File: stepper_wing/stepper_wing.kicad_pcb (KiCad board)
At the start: 2 copper layers, 47 x 49.5 mm, 40 parts, among them U1 MCP44X1, U2 MCP23017, U3 DRV8825, U4 DRV8825, U5 DRV8825, U6 DRV8825

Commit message: try alt layout
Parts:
- removed the Nylon Only at (106.4, 80.5)
- removed the Nylon Only at (106.4, 122.4)
- removed WINGPWR1: WINGPWR, Connect:bornier2
- added P1: CONN_1, Local:TabRA, F.Cu at (145.8, 97.0)
- added P2: CONN_1, Local:TabRA, F.Cu at (145.8, 105.9)
- C1, C10, C12, C13, C2, C3, C4, C6, C7, C9: footprint SMD_Packages:SMD-0603_c -> Local:0805C
- C11, C14, C5, C8: footprint SMD_Packages:SMD-0603_c -> Local:0805C; moved to B.Cu
- R1, R2: footprint SMD_Packages:SMD-0603_r -> Local:0805R
- R10, R3, R4, R5, R6, R7, R8, R9: footprint Resistors_SMD:Resistor_SMD2512_HandSoldering -> Resistors_SMD:R_2512
- STEP1, STEP2, STEP3, STEP4: footprint Pin_Headers:Pin_Header_Angled_1x04 -> Pin_Headers:Pin_Header_Straight_1x04
- moved C2 29.8 mm to (110.9, 127.4), turned to 0 degrees
- moved U2 15.9 mm to (109.0, 117.3), turned to 90 degrees
- moved C5 6.91 mm to (121.4, 117.0), turned to 270 degrees
- moved R1 6.59 mm to (114.0, 85.6), turned to 90 degrees
- moved C8 6.56 mm to (121.4, 104.9), turned to 270 degrees
- moved C13 6.35 mm to (126.4, 88.8)
- moved C10 6.26 mm to (126.4, 100.8)
- moved C11 6.25 mm to (121.4, 92.8), turned to 270 degrees
- moved C4 6.23 mm to (126.4, 125.0)
- moved C7 6.22 mm to (126.4, 112.9)
- moved C14 6.04 mm to (121.4, 80.8), turned to 270 degrees
- moved R2 5.38 mm to (109.0, 89.4)
- moved STEP4 5.24 mm to (135.6, 83.1), turned to 180 degrees
- moved U1 5.24 mm to (109.0, 84.3)
- moved U6 5.24 mm to (124.2, 83.1)
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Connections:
- U2 pad 1: /Stepper2/MODE2 -> /Stepper1/MODE2
- U2 pad 2: /Stepper2/MODE1 -> /Stepper1/MODE1
- U2 pad 21: /Stepper0/MODE2 -> /Stepper3/DECAY
- U2 pad 22: /Stepper0/MODE1 -> /Stepper3/MODE0
- U2 pad 23: /Stepper0/MODE0 -> /Stepper3/MODE1
- U2 pad 24: /Stepper0/DECAY -> /Stepper3/MODE2
- U2 pad 25: /Stepper1/MODE2 -> /Stepper0/DECAY
- U2 pad 26: /Stepper1/MODE1 -> /Stepper0/MODE0
- U2 pad 27: /Stepper1/MODE0 -> /Stepper0/MODE1
- U2 pad 28: /Stepper1/DECAY -> /Stepper0/MODE2
- U2 pad 3: /Stepper2/MODE0 -> /Stepper1/MODE0
- U2 pad 4: /Stepper2/DECAY -> /Stepper1/DECAY
- U2 pad 5: /Stepper3/MODE2 -> /Stepper2/MODE2
- U2 pad 6: /Stepper3/MODE1 -> /Stepper2/MODE1
- U2 pad 7: /Stepper3/MODE0 -> /Stepper2/MODE0
- U2 pad 8: /Stepper3/DECAY -> /Stepper2/DECAY
- U3 pad 16: Net-(C5-Pad1) -> +3.3V
- U3 pad 17: Net-(C5-Pad1) -> +3.3V
- U3 pad 5: Net-(STEP1-Pad4) -> Net-(STEP1-Pad3)
- U3 pad 7: Net-(STEP1-Pad3) -> Net-(STEP1-Pad4)
- U4 pad 16: Net-(C8-Pad1) -> +3.3V
- U4 pad 17: Net-(C8-Pad1) -> +3.3V
- U4 pad 5: Net-(STEP2-Pad4) -> Net-(STEP2-Pad3)
- U4 pad 7: Net-(STEP2-Pad3) -> Net-(STEP2-Pad4)
- U5 pad 16: Net-(C11-Pad1) -> +3.3V
- U5 pad 17: Net-(C11-Pad1) -> +3.3V
- U5 pad 5: Net-(STEP3-Pad4) -> Net-(STEP3-Pad3)
- U5 pad 7: Net-(STEP3-Pad3) -> Net-(STEP3-Pad4)
- U6 pad 16: Net-(C14-Pad1) -> +3.3V
- U6 pad 17: Net-(C14-Pad1) -> +3.3V
- U6 pad 5: Net-(STEP4-Pad4) -> Net-(STEP4-Pad3)
- U6 pad 7: Net-(STEP4-Pad3) -> Net-(STEP4-Pad4)
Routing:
- net GND: track 105.9 -> 32.6 mm, vias 66 -> 4
- net /Stepper0/PW: track 80.9 -> 9.35 mm, vias 2 -> 0
- net +3.3V: track 69.4 -> 103.7 mm, vias 0 -> 2
- net /Stepper1/PW: track 91.3 -> 63.7 mm
- net /Stepper3/MODE2: track 16.5 -> 43.3 mm
- net /Stepper3/MODE0: track 19.0 -> 42.9 mm
- net /Stepper3/MODE1: track 17.8 -> 41.6 mm
- net /Stepper3/DECAY: track 23.8 -> 46.6 mm
- net /Stepper2/MODE2: track 6.18 -> 28.5 mm
- net /Stepper2/DECAY: track 13.6 -> 35.0 mm
- net /Stepper2/MODE1: track 7.69 -> 28.9 mm
- net /SDA: track 28.8 -> 50.0 mm, vias 0 -> 1
- net /SCL: track 32.4 -> 53.5 mm, vias 0 -> 1
- net /Stepper1/DECAY: track 8.54 -> 28.2 mm
- net /Stepper2/MODE0: track 8.82 -> 28.5 mm
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- removed copper zone on F.Cu, net Net-(STEP1-Pad1)
- removed copper zone on F.Cu, net Net-(STEP1-Pad2)
- removed copper zone on F.Cu, net Net-(STEP1-Pad3)
- removed copper zone on F.Cu, net Net-(STEP1-Pad4)
- removed copper zone on F.Cu, net Net-(STEP2-Pad1)
- removed copper zone on F.Cu, net Net-(STEP2-Pad2)
- removed copper zone on F.Cu, net Net-(STEP2-Pad3)
- removed copper zone on F.Cu, net Net-(STEP2-Pad4)
- removed copper zone on F.Cu, net Net-(STEP3-Pad1)
- removed copper zone on F.Cu, net Net-(STEP3-Pad2)
- removed copper zone on F.Cu, net Net-(STEP3-Pad3)
- removed copper zone on F.Cu, net Net-(STEP3-Pad4)
- removed copper zone on F.Cu, net Net-(STEP4-Pad1)
- removed copper zone on F.Cu, net Net-(STEP4-Pad2)
- removed copper zone on F.Cu, net Net-(STEP4-Pad3)
- removed copper zone on F.Cu, net Net-(STEP4-Pad4)
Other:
- net class Default: trace_width 0.4318 -> 0.4

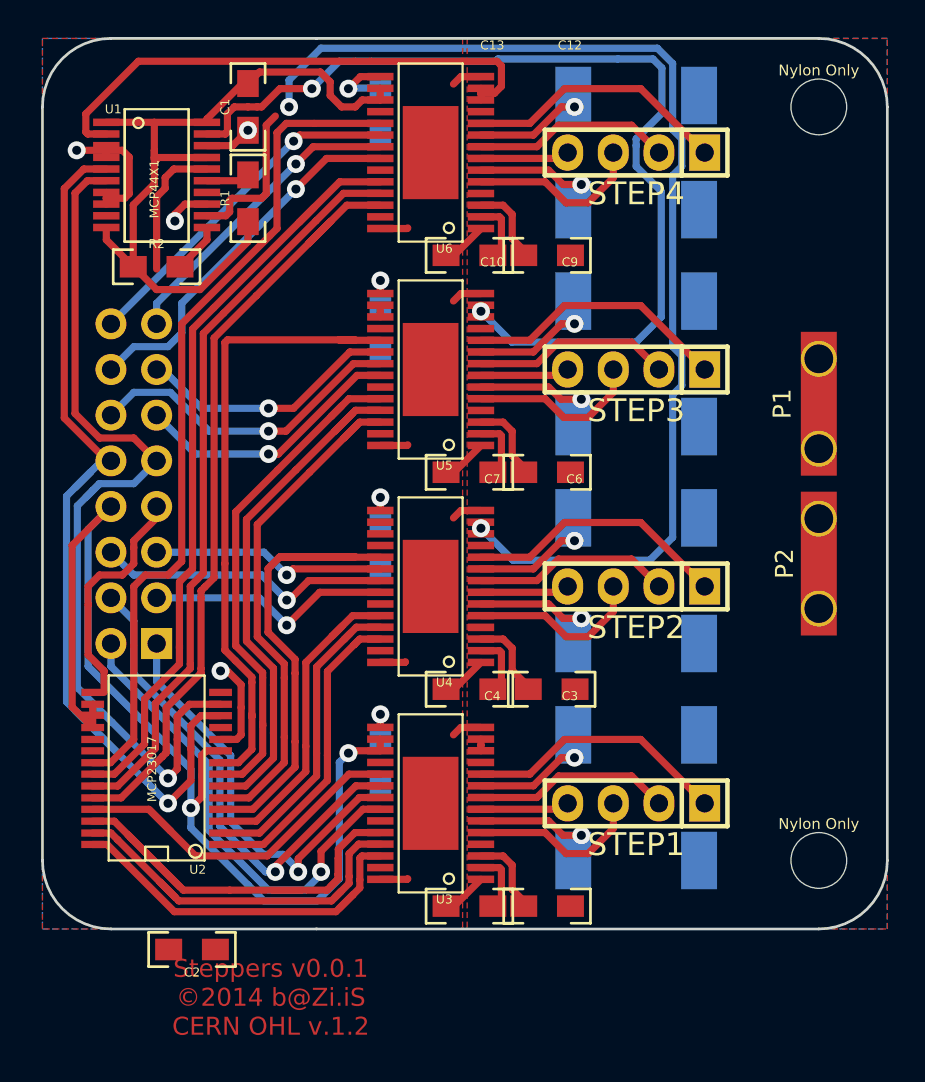
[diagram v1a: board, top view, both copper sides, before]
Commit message: need to enbigen silk
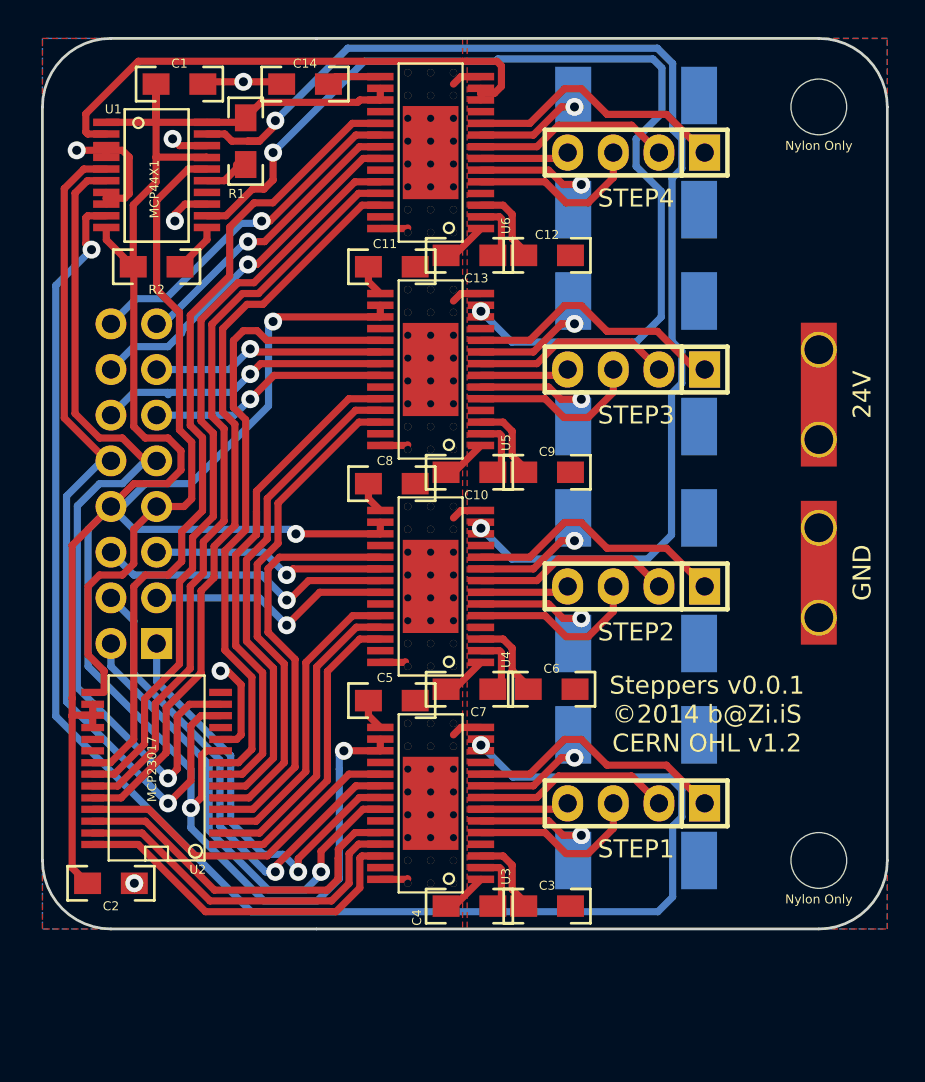
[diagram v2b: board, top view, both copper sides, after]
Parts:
- C11, C14, C5, C8: moved to F.Cu
- M1, M2: renamed from Nylon Only; value 3-1mm -> Nylon Only
- P1: value CONN_1 -> 24V
- P2: value CONN_1 -> GND
- moved C2 5.82 mm to (106.4, 123.7)
- moved C14 4.46 mm to (117.2, 79.2), turned to 180 degrees
- moved C1 4.02 mm to (110.2, 79.2), turned to 0 degrees
- moved C11 3.49 mm to (122.0, 89.4), turned to 0 degrees
- moved C5 3.49 mm to (122.0, 113.5), turned to 0 degrees
- moved C8 3.49 mm to (122.0, 101.5), turned to 0 degrees
- moved R1 3.18 mm to (113.9, 82.4), turned to 270 degrees
- moved P1 0.51 mm to (145.8, 96.5)
- moved P2 0.51 mm to (145.8, 106.4)
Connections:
- U1 pad 12: /Stepper0/PW -> /Stepper2/PW
- U1 pad 19: /Stepper2/PW -> /Stepper1/PW
- U1 pad 9: /Stepper1/PW -> /Stepper0/PW
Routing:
- net /Stepper0/PW: track 9.35 -> 88.0 mm, vias 0 -> 2
- net +3.3V: track 103.7 -> 161.8 mm, vias 2 -> 4
- net /ADD: track 21.5 -> 36.7 mm
- net /Stepper1/PW: track 63.7 -> 69.0 mm
- net /SCL: track 53.5 -> 48.6 mm
- net /Stepper1/DECAY: track 28.2 -> 23.3 mm
- net /Stepper0/MODE0: track 25.9 -> 21.0 mm
- net GND: track 32.6 -> 36.9 mm, vias 4 -> 6
- net /Stepper2/PW: track 54.8 -> 57.0 mm
- net /Stepper2/STEP: track 15.1 -> 13.4 mm
- net /Stepper0/MODE1: track 21.5 -> 19.8 mm
- net /Stepper0/DECAY: track 20.6 -> 19.0 mm
- net /Stepper2/EN: track 18.0 -> 16.3 mm
- net /Stepper2/MODE1: track 28.9 -> 27.4 mm
- net /Stepper2/DIR: track 14.6 -> 13.3 mm
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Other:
- rule pad_to_mask_clearance: 0.2 -> 0
- board text added: "Steppers v0.0.1 ©2014 b@Zi.iS CERN OHL v1.2"
- board text removed: "Steppers v0.0.1 ©2014 b@Zi.iS CERN OHL v.1.2"

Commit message: tidy
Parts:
- M1, M2: value Nylon Only -> Nylon
- U2: footprint SMD_Packages:SSOP-28 -> Local:SSOP-28
- moved C14 2.67 mm to (114.6, 79.1)
- moved C1 1.91 mm to (108.3, 79.1)
- moved R2 0.92 mm to (109.2, 88.5)
- moved U1 0.90 mm to (108.3, 83.7)
- moved U2 0.77 mm to (108.2, 117.2)
- moved R1 0.63 mm to (113.4, 82.0)
- moved C2 0.51 mm to (106.4, 124.2)
- moved C10 0.38 mm to (126.7, 100.8)
- moved C13 0.38 mm to (126.7, 88.8)
- moved C4 0.38 mm to (126.7, 125.0)
- moved C7 0.38 mm to (126.7, 112.9)
- moved C12 0.13 mm to (130.8, 88.8)
- moved C3 0.13 mm to (130.8, 125.0)
- moved C6 0.13 mm to (130.8, 112.9)
- moved C9 0.13 mm to (130.8, 100.8)
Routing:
- net /Stepper0/PW: track 88.0 -> 99.1 mm
- net GND: track 36.9 -> 43.0 mm, vias 6 -> 5
- net /SCL: track 48.6 -> 43.1 mm
- net /Stepper1/PW: track 69.0 -> 74.2 mm
- net /Stepper2/PW: track 57.0 -> 62.1 mm
- net +3.3V: track 161.8 -> 157.1 mm, vias 4 -> 6
- net /Stepper3/PW: track 29.7 -> 32.9 mm
- net /SDA: track 48.9 -> 45.9 mm
- net /Stepper3/DECAY: track 45.6 -> 48.5 mm
- net Net-(C14-Pad1): track 3.06 -> 5.82 mm
- net /Stepper3/MODE1: track 42.2 -> 44.5 mm
- net /Stepper2/DECAY: track 34.8 -> 32.5 mm
- net /Stepper0/STEP: track 26.2 -> 28.4 mm
- net /Stepper1/DECAY: track 23.3 -> 21.3 mm
- net /Stepper3/MODE2: track 42.2 -> 44.0 mm
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
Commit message: more titdy
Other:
- net class Default: via_drill 0.5 -> 0.4
